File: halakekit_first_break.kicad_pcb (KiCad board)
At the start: 2 copper layers, 45.7 x 38.1 mm, 30 parts, among them J1 HEADER_3, J10 HEADER_3, J11 HEADER_3, J12 HEADER_3, J13 HEADER_3, J14 HEADER_3, J15 HEADER_3, J16 HEADER_3, J17 HEADER_3, J18 HEADER_3, J19 HEADER_3, J2 HEADER_3, J20 HEADER_3, J21 HEADER_10, J22 HEADER_10, J23 HEADER_2x2, J24 HEADER_4, J25 HEADER_12, J26 HEADER_2, J27 HEADER_12, J28 HEADER_4, J3 HEADER_3, J4 HEADER_3, J5 HEADER_3, J6 HEADER_3, J7 HEADER_3, J8 HEADER_3, J9 HEADER_3, U1 Arduino_Pro_Micro

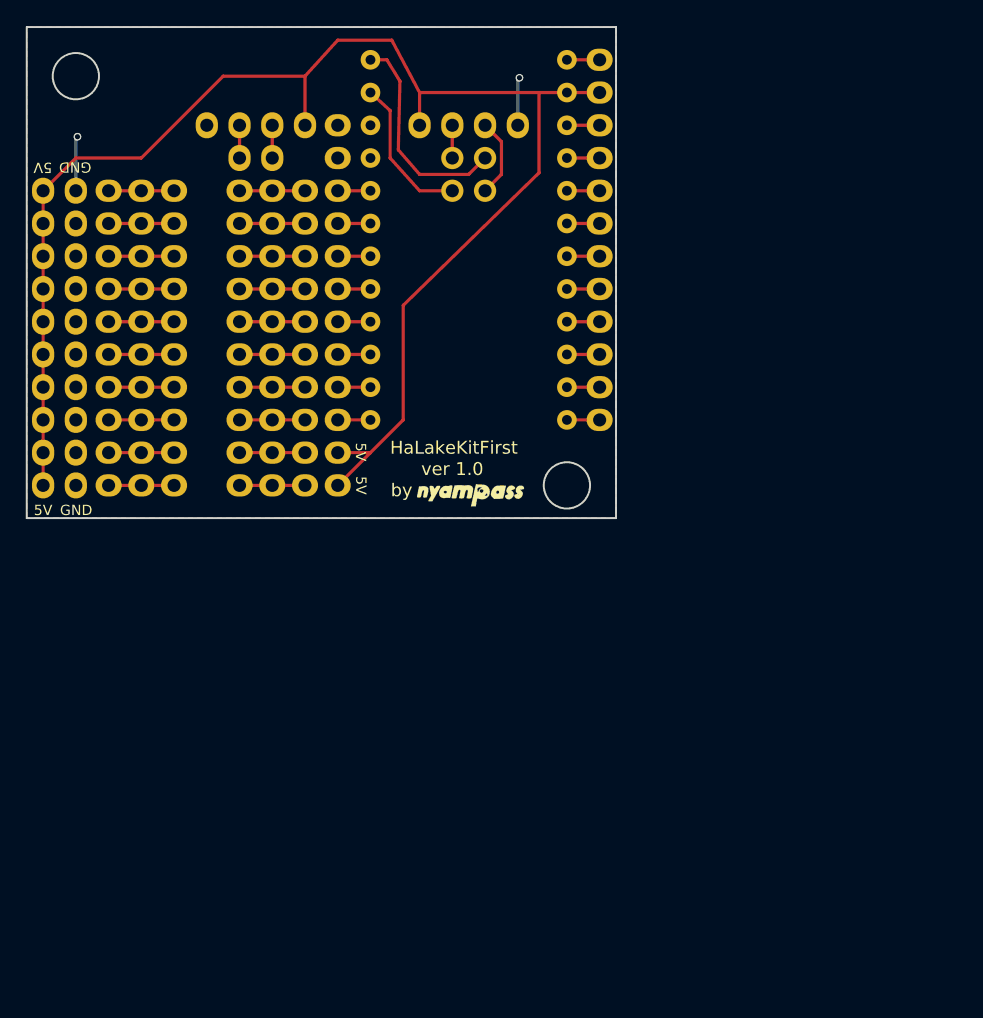
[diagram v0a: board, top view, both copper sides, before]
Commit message: Update schema for rev1.1
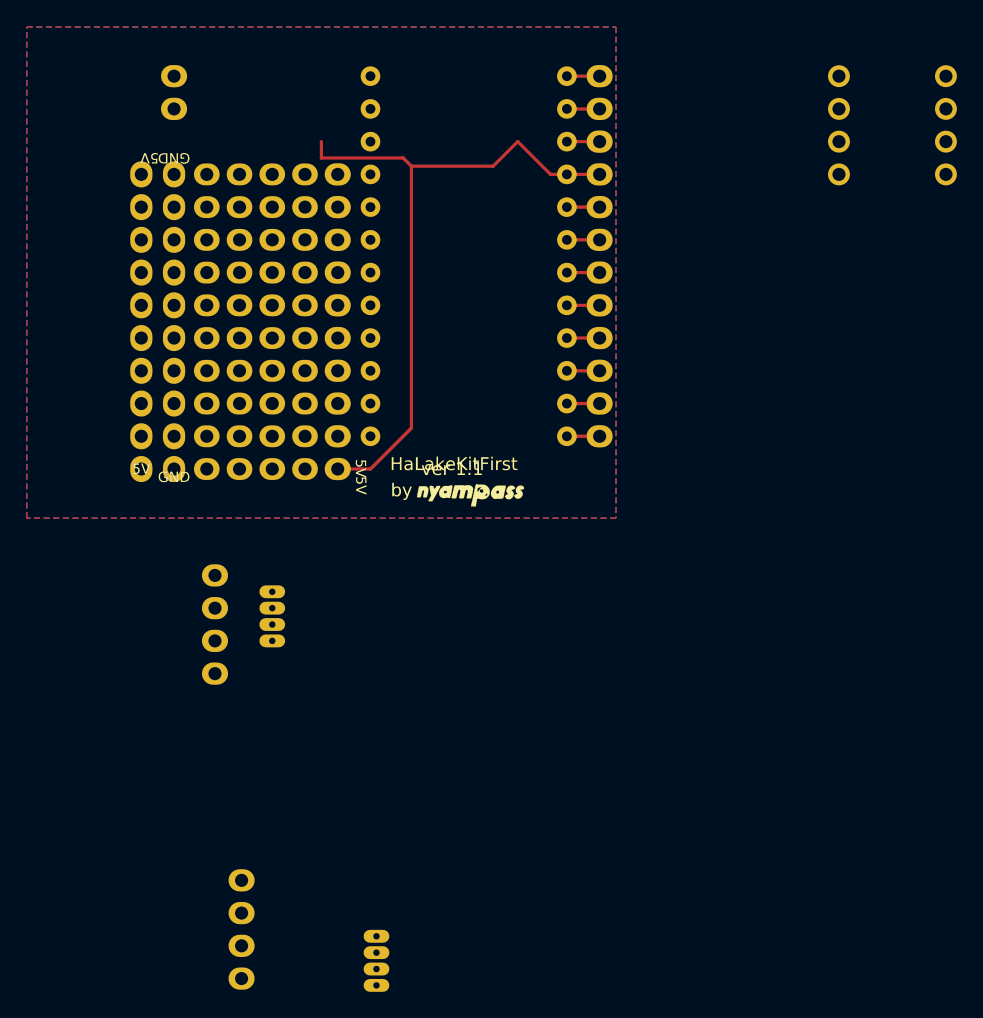
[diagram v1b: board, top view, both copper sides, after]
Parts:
- removed J16, J17, J18, J19, J20: HEADER_3, simple_headers:Pin_Header_Straight_1x03
- removed J23: HEADER_2x2, simple_headers:Pin_Header_Straight_2x02
- removed J25: HEADER_12, simple_headers:Pin_Header_Straight_1x12
- J1, J11, J12, J13, J14, J15, J2, J3, J4, J5: value HEADER_3 -> LINE_4; footprint simple_headers:Pin_Header_Straight_1x03 -> simple_headers:Pin_Header_Connect_1x04
- J10, J9: value HEADER_3 -> Connector_4; footprint simple_headers:Pin_Header_Straight_1x03 -> simple_headers:Pin_Header_Straight_1x04
- J21, J22: value HEADER_10 -> LINE_10
- J24, J28: value HEADER_4 -> CIRCLES_4; footprint simple_headers:Pin_Header_Straight_1x04 -> simple_headers:Pin_Header_Circle_1x04
- J6: value HEADER_3 -> HEADER_10; footprint simple_headers:Pin_Header_Straight_1x03 -> simple_headers:Pin_Header_Straight_1x10
- J7, J8: value HEADER_3 -> Connector_s_4; footprint simple_headers:Pin_Header_Straight_1x03 -> simple_headers:headers_s_4
- moved J28 49.9 mm to (186.9, 106.7), turned to 0 degrees
- moved J8 45.1 mm to (142.7, 173.4)
- moved J24 32.8 mm to (178.6, 106.7), turned to 0 degrees
- moved J10 32.3 mm to (132.2, 169.1)
- moved J6 22.6 mm to (139.7, 114.3)
- moved J7 20.3 mm to (134.6, 146.7)
- moved J13 14.2 mm to (129.5, 134.6), turned to 90 degrees
- moved J9 12.6 mm to (130.2, 145.4)
- moved J4 11.7 mm to (129.5, 132.1), turned to 90 degrees
- moved J15 11.7 mm to (129.5, 137.2), turned to 90 degrees
- moved J11 9.25 mm to (129.5, 124.5), turned to 90 degrees
- moved J12 9.25 mm to (129.5, 127.0), turned to 90 degrees
- moved J5 8.52 mm to (129.5, 121.9), turned to 90 degrees
- moved J26 8.13 mm to (127.0, 106.7), turned to 0 degrees
- moved J21 7.73 mm to (127.0, 137.2)
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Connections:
- J10 pad 1: Net-(J10-Pad1) -> Connector2_5V
- J10 pad 2: Net-(J10-Pad1) -> Connector2_RX
- J10 pad 3: Net-(J10-Pad1) -> Connector2_TX
- J24 pad 2: RX(TX) -> RXD
- J24 pad 3: TX(RX) -> TXD
- J27 pad 2: +5V -> GND
- J27 pad 4: GND -> +5V
- J6 pad 1: Net-(J6-Pad1) -> GND
- J6 pad 2: Net-(J6-Pad1) -> 2
- J6 pad 3: Net-(J6-Pad1) -> 3
- J7 pad 1: Net-(J7-Pad1) -> Connector1_5V
- J7 pad 2: Net-(J7-Pad1) -> Connector1_RX
- J7 pad 3: Net-(J7-Pad1) -> Connector1_TX
- J8 pad 1: Net-(J8-Pad1) -> Connector2_5V
- J8 pad 2: Net-(J8-Pad1) -> Connector2_RX
- J8 pad 3: Net-(J8-Pad1) -> Connector2_TX
- J9 pad 1: Net-(J9-Pad1) -> Connector1_5V
- J9 pad 2: Net-(J9-Pad1) -> Connector1_RX
- J9 pad 3: Net-(J9-Pad1) -> Connector1_TX
- U1 pad 21: GND -> +5V
- U1 pad 23: +5V -> GND
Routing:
- net +5V: track 119.3 -> 52.3 mm
- net TXD: track 16.7 -> 0.25 mm
- net RXD: track 11.7 -> 0.51 mm
- net GND: track 10.8 -> 2.54 mm, vias 2 -> 0
- net TX(RX): track 6.13 -> 0.00 mm
- net Net-(J9-Pad1): track 5.08 -> 0.00 mm
- net Net-(J8-Pad1): track 5.08 -> 0.00 mm
- net Net-(J7-Pad1): track 5.08 -> 0.00 mm
- net Net-(J6-Pad1): track 5.08 -> 0.00 mm
- net Net-(J5-Pad1): track 5.08 -> 0.00 mm
- net Net-(J4-Pad1): track 5.08 -> 0.00 mm
- net Net-(J3-Pad1): track 5.08 -> 0.00 mm
- net Net-(J2-Pad1): track 5.08 -> 0.00 mm
- net Net-(J10-Pad1): track 5.08 -> 0.00 mm
- net Net-(J1-Pad1): track 5.08 -> 0.00 mm
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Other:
- board outline removed
- net class Default: clearance 0.2 -> 0.15
- rule trace_clearance: 0.2 -> 0.15
- board text added: "ver 1.1"
- board text removed: "ver 1.0"

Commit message: Update PCB and plot files to Rev.1.1
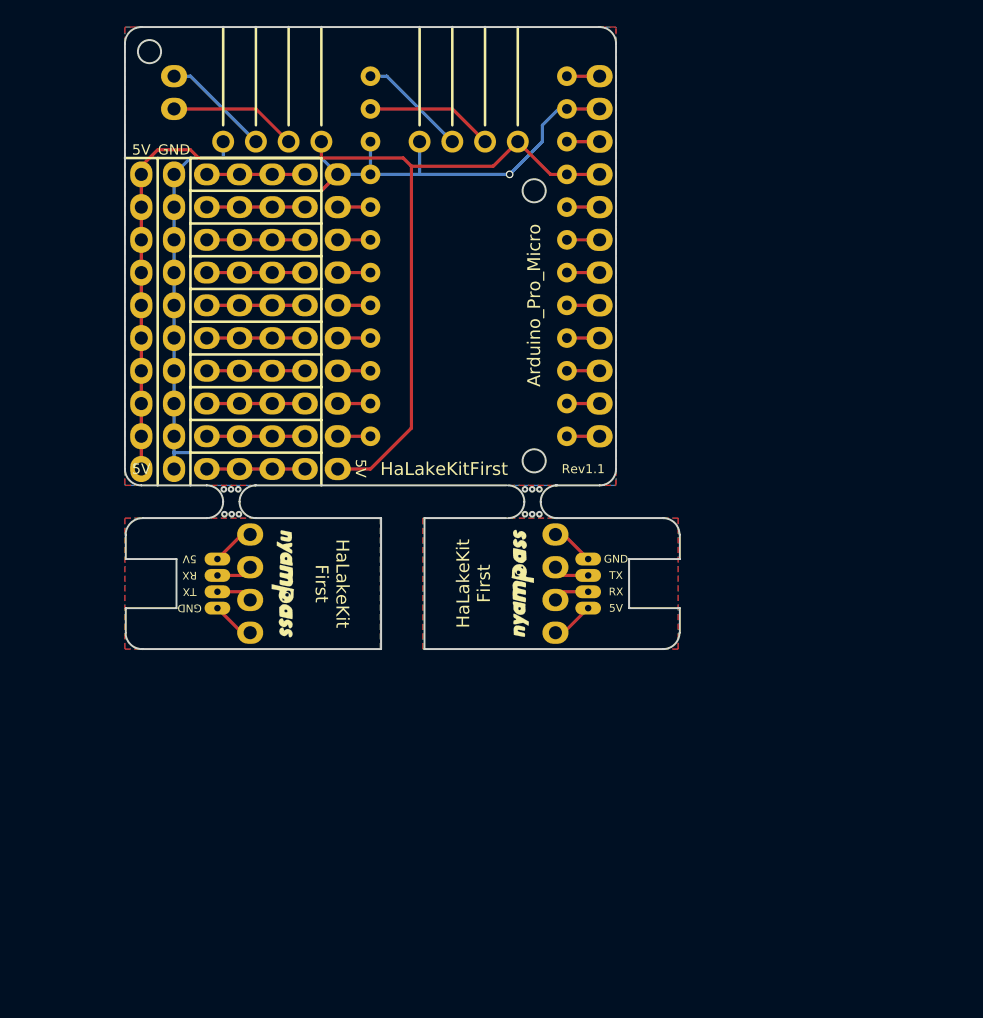
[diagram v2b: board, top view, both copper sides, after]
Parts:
- added G***: LOGO, logos:nyampass_logo_8p4mm, B.Cu at (144.7, 118.8)
- added G***: LOGO, logos:nyampass_logo_8p4mm, F.Cu at (154.1, 146.1)
- moved J28 48.7 mm to (138.4, 111.8), turned to 270 degrees
- moved J10 31.0 mm to (156.6, 149.9), turned to 180 degrees
- moved J8 30.3 mm to (159.1, 148.0), turned to 180 degrees
- moved J24 25.4 mm to (153.7, 111.8), turned to 270 degrees
- moved G*** 16.1 mm to (135.4, 146.1), turned to 270 degrees
- moved J7 4.96 mm to (130.4, 144.1)
- moved J9 4.19 mm to (132.9, 142.2)
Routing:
- net GND: track 2.54 -> 71.0 mm, vias 0 -> 1
- net +5V: track 52.3 -> 90.6 mm
- net RXD: track 0.51 -> 10.5 mm
- net Net-(J26-Pad2): track 0.00 -> 9.94 mm
- net Net-(J26-Pad1): track 0.00 -> 8.45 mm
- net TXD: track 0.25 -> 8.71 mm
- net Net-(J5-Pad1): track 0.00 -> 7.62 mm
- net Net-(J4-Pad1): track 0.00 -> 7.62 mm
- net Net-(J3-Pad1): track 0.00 -> 7.62 mm
- net Net-(J2-Pad1): track 0.00 -> 7.62 mm
- net Net-(J15-Pad1): track 0.00 -> 7.62 mm
- net Net-(J14-Pad1): track 0.00 -> 7.62 mm
- net Net-(J13-Pad1): track 0.00 -> 7.62 mm
- net Net-(J12-Pad1): track 0.00 -> 7.62 mm
- net Net-(J11-Pad1): track 0.00 -> 7.62 mm
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- added copper zone on B.Cu, net Connector1_GND
- added copper zone on F.Cu, net Connector1_GND
- added copper zone on B.Cu, net Connector2_GND
- added copper zone on F.Cu, net Connector2_GND
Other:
- board outline added: 43.1 x 48.3 mm
- board text added: "HaLakeKit First"
- board text added: "RX"
- board text added: "Rev1.1"
- board text added: "TX"
- board text removed: "by"
- board text removed: "ver 1.1"

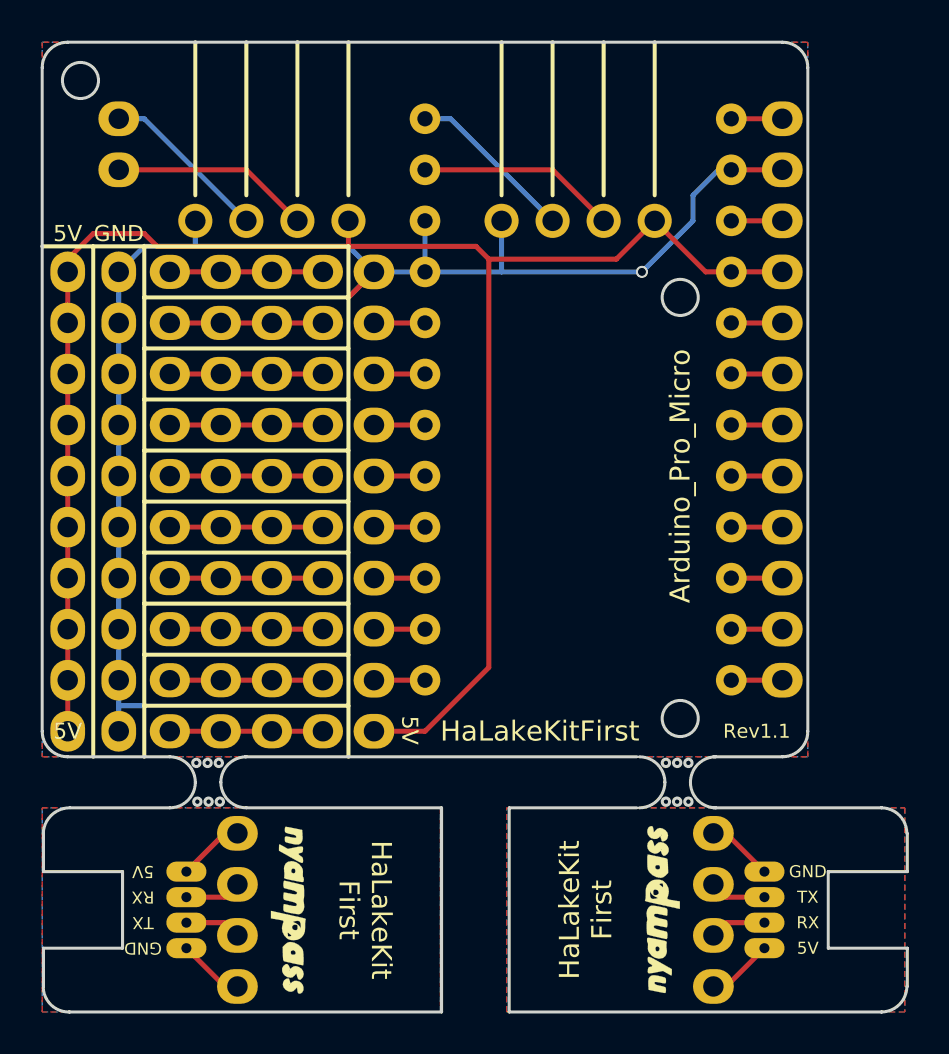
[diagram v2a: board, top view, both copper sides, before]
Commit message: Change size of holl and connector footprint larger
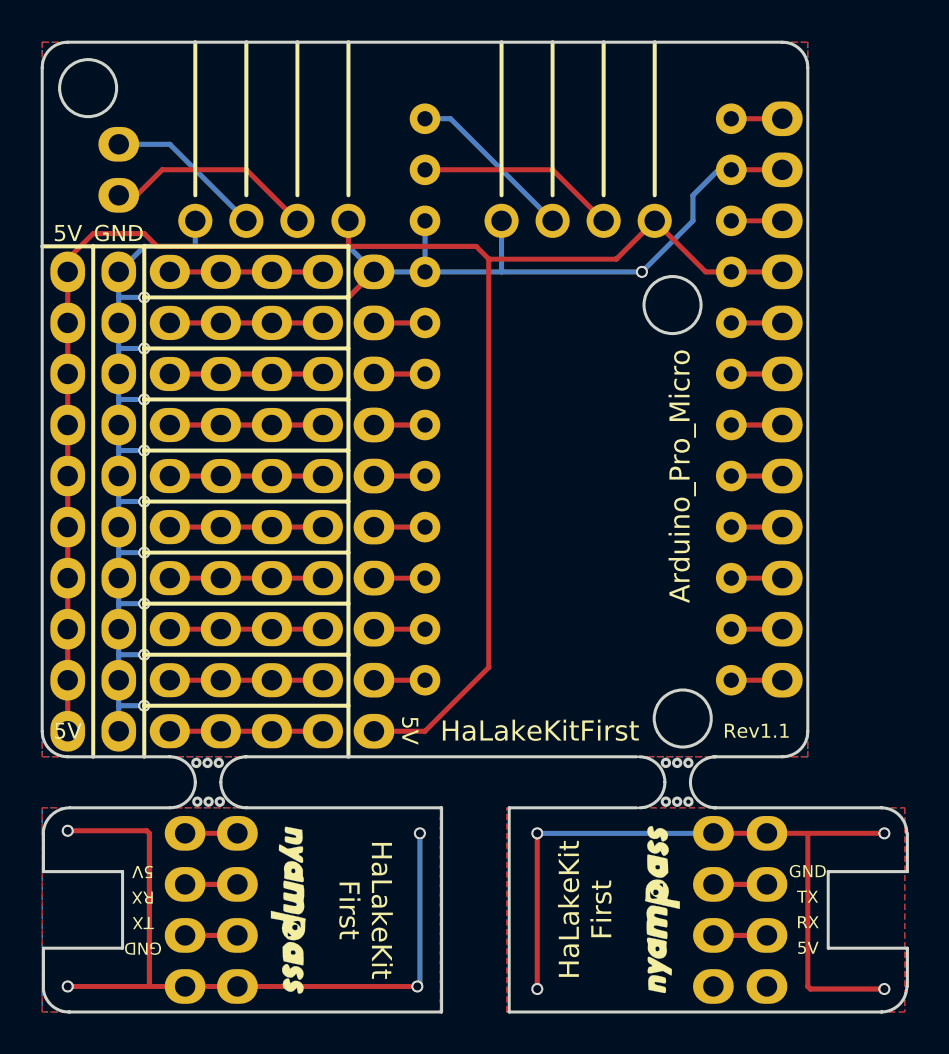
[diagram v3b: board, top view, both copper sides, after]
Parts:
- J7, J8: value Connector_s_4 -> Connector_4; footprint simple_headers:headers_s_4 -> simple_headers:Pin_Header_Straight_1x04
- moved J8 1.91 mm to (159.3, 149.9)
- moved J7 1.91 mm to (130.3, 142.2)
- moved J26 1.27 mm to (127.0, 108.0)
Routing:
- net Connector1_GND: track 3.33 -> 37.4 mm, vias 0 -> 4
- net Connector2_GND: track 3.33 -> 37.4 mm, vias 0 -> 4
- net GND: track 71.0 -> 81.5 mm, vias 1 -> 10
- net Connector2_5V: track 3.33 -> 0.63 mm
- net Net-(J26-Pad1): track 8.45 -> 7.93 mm
- net Net-(J26-Pad2): track 9.94 -> 10.5 mm
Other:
- outline, holes or cut-outs redrawn
